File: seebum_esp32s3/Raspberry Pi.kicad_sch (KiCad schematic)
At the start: 1 part, among them J401 GPIO

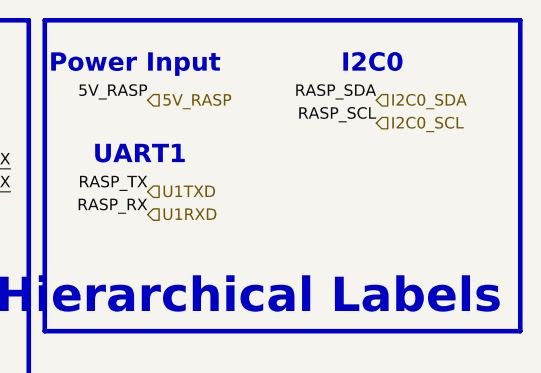
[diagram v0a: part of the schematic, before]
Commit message: Feat: fix uart1 schematic issue and I2C redundancy
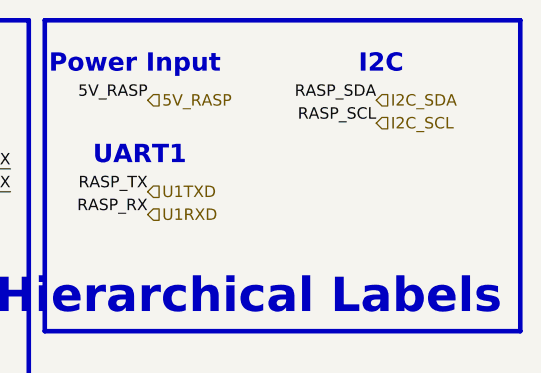
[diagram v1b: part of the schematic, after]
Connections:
- net I2C0_SCL renamed I2C_SCL
- net I2C0_SDA renamed I2C_SDA
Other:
- note added: "I2C"
- note removed: "I2C0"
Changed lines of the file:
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@@
 		)
 	)
-	(text "I2C0"
+	(text "I2C"
 		(exclude_from_sim no)
 		(at 100.838 20.066 0)
@@
 		)
 	)
-	(hierarchical_label "I2C0_SCL"
+	(hierarchical_label "I2C_SCL"
 		(shape input)
 		(at 97.79 25.4 0)
@@
 		)
 	)
-	(hierarchical_label "I2C0_SDA"
+	(hierarchical_label "I2C_SDA"
 		(shape input)
 		(at 97.79 22.86 0)

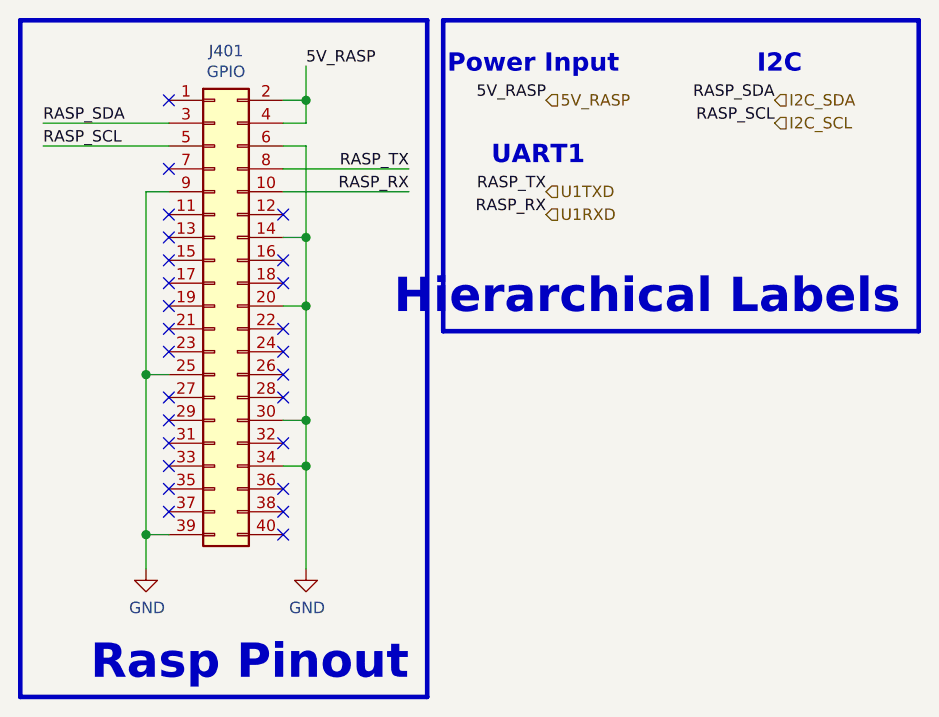
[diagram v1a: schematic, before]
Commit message: Feat: I2C and UART to same pins in ESP32, since any GPIO can be RxD and TxD
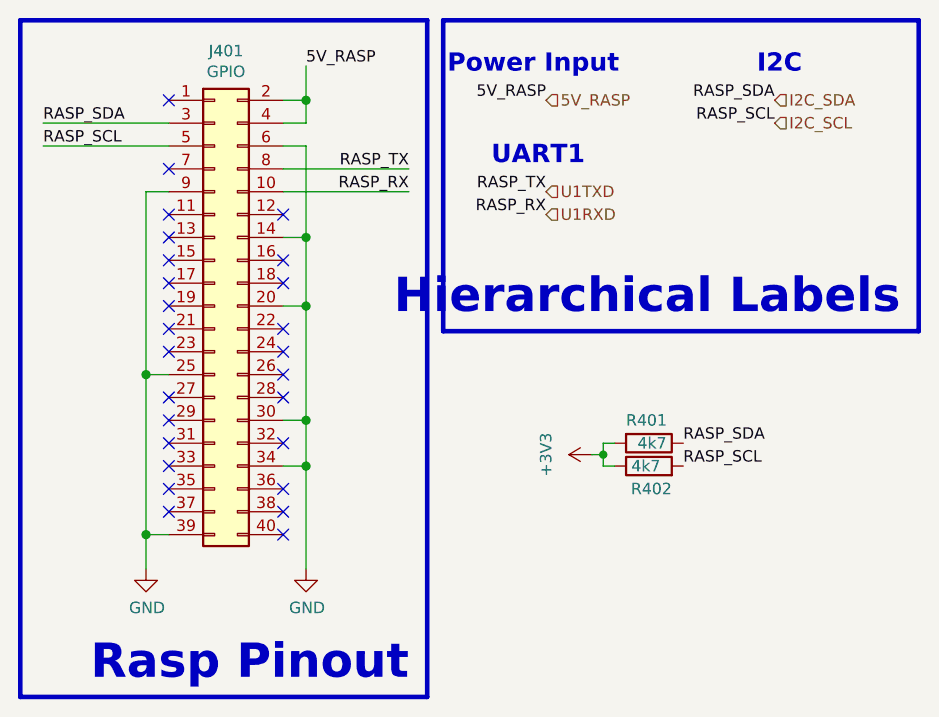
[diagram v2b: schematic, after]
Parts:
- added R401, R402: 4k7, Resistor_SMD:R_0805_2012Metric, symbol Device:R
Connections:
- net I2C_SCL: now also R402.2
- net I2C_SDA: now also R401.1
- new net +3V3: R401.2, R402.1
